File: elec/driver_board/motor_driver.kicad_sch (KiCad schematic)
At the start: 7 parts, among them IC25 MC74HC595ADR2G-Q, IC26 TPL7407LADR, IC27 TPL7407LADR, J15 MOTOR_1, J16 MOTOR_0

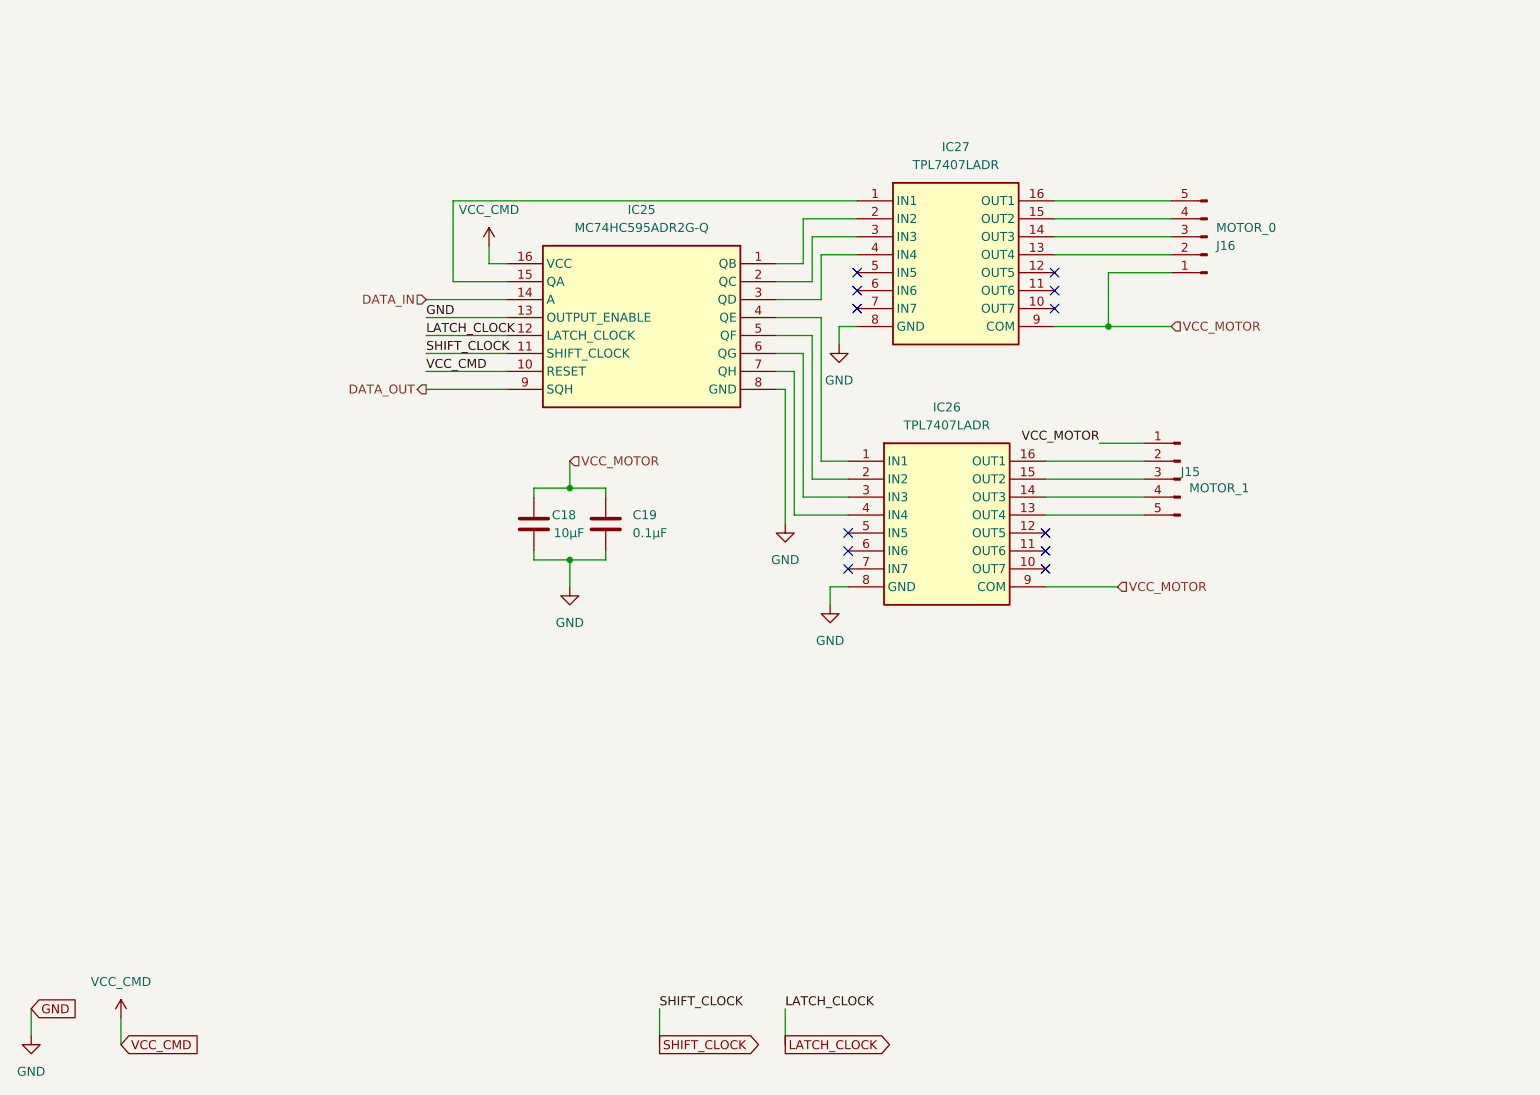
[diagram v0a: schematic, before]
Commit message: [elec] New design with BKA30D-R5
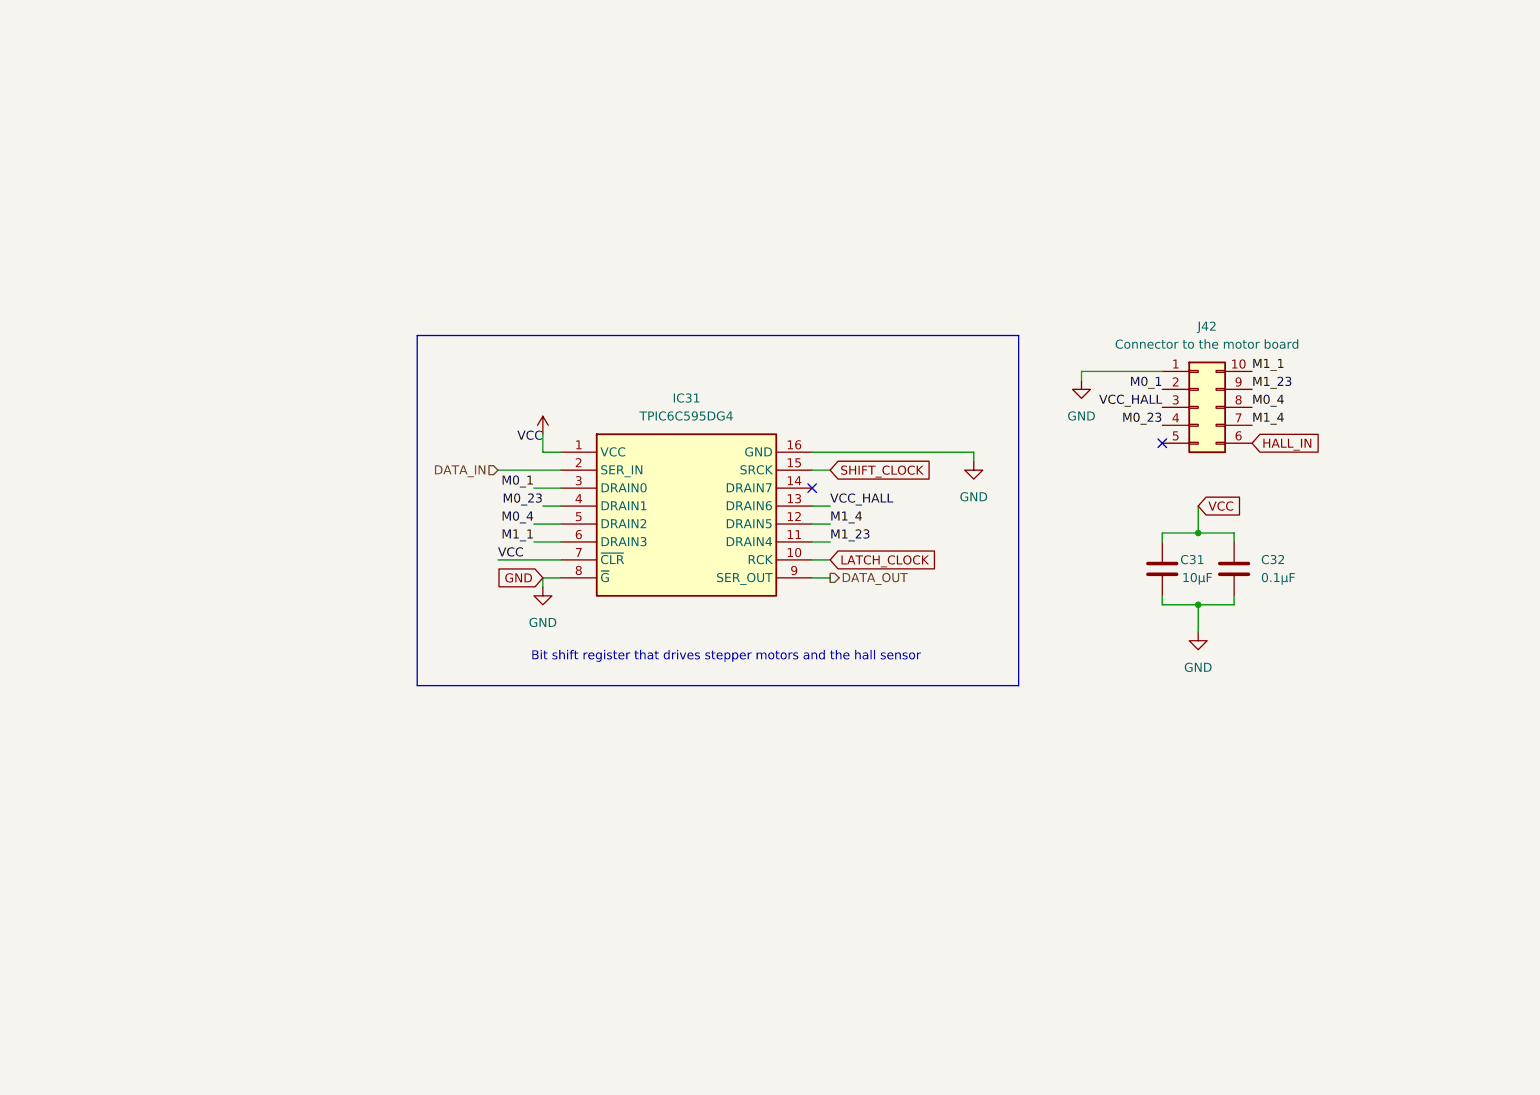
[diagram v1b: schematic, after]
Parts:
- removed IC25: MC74HC595ADR2G-Q, Samacsys:SOIC127P600X175-16N, symbol Samacsys:MC74HC595ADR2G-Q
- removed IC26, IC27: TPL7407LADR, Samacsys:SOIC127P600X175-16N, symbol Samacsys:TPL7407LADR
- removed J15: MOTOR_1, Connector_PinHeader_2.54mm:PinHeader_1x05_P2.54mm_Vertical, symbol Connector:Conn_01x05_Pin
- removed J16: MOTOR_0, Connector_PinHeader_2.54mm:PinHeader_1x05_P2.54mm_Vertical, symbol Connector:Conn_01x05_Pin
- added IC31: TPIC6C595DG4, Samacsys:SOIC127P600X175-16N, symbol Samacsys:TPIC6C595DG4
- added J42: Connector to the motor board, Connector_IDC:IDC-Header_2x05_P2.54mm_Vertical, symbol Connector_Generic:Conn_02x05_Counter_Clockwise
- renumbered C18 to C31, C19 to C32
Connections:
- net VCC_MOTOR is gone; now on net VCC_CMD: C31.1, C32.1
- net DATA_IN: now also IC31.2 (SER_IN)
- net DATA_OUT: now also IC31.9 (SER_OUT)
- net GND: now also IC31.16 (GND), IC31.8 (~{G}), J42.1 (Pin_1)
- net LATCH_CLOCK: now also IC31.10 (RCK)
- net SHIFT_CLOCK: now also IC31.15 (SRCK)
- net VCC_CMD: now also IC31.1 (VCC), IC31.7 (~{CLR})
- new net HALL_IN: J42.6 (Pin_6)
- new net M0_1: IC31.3 (DRAIN0), J42.2 (Pin_2)
- new net M0_23: IC31.4 (DRAIN1), J42.4 (Pin_4)
- new net M0_4: IC31.5 (DRAIN2), J42.8 (Pin_8)
- new net M1_1: IC31.6 (DRAIN3), J42.10 (Pin_10)
- new net M1_23: IC31.11 (DRAIN4), J42.9 (Pin_9)
- new net M1_4: IC31.12 (DRAIN5), J42.7 (Pin_7)
- new net VCC_HALL: IC31.13 (DRAIN6), J42.3 (Pin_3)
- no-connect marks 12 -> 2
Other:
- note added: "Bit shift register that drives stepper motors and the hall sensor"
- title: (none) -> Motor driver
- moved on the sheet: C31, C32

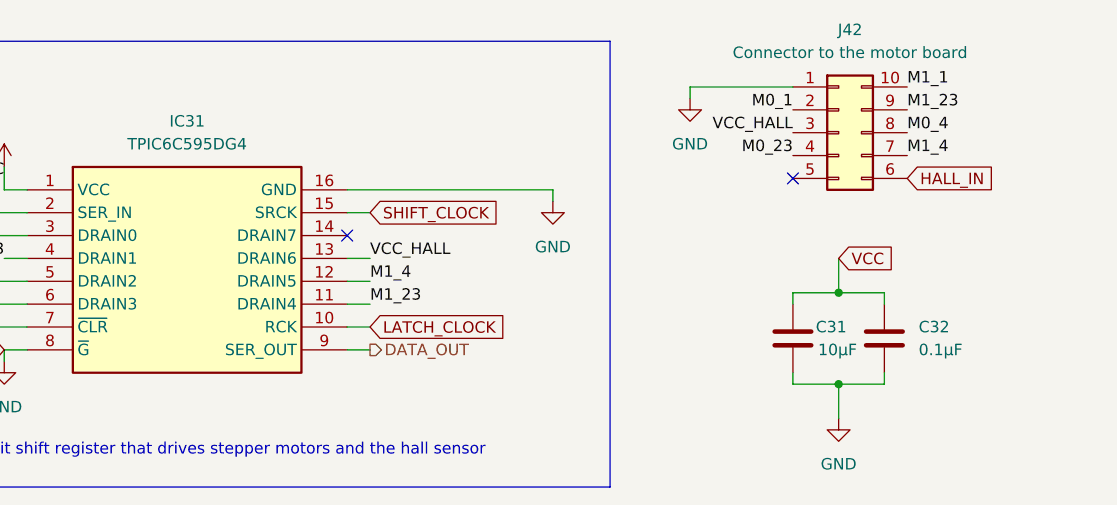
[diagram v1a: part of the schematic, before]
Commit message: [elec] continue routing
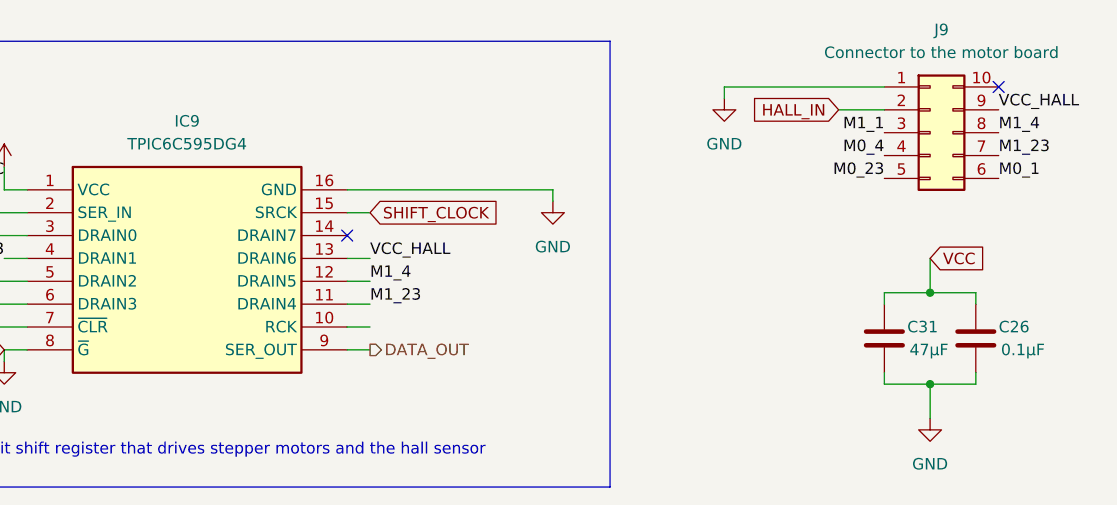
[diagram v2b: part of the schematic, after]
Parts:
- removed C32: 0.1µF, Snapeda:1808J1000392KCT_CAPC4520X200N, symbol Device:C
- added C26: 0.1µF, Capacitor_SMD:C_1210_3225Metric_Pad1.33x2.70mm_HandSolder, symbol Device:C
- C31: value 10µF -> 47µF; footprint Capacitor_SMD:C_1210_3225Metric -> Capacitor_SMD:C_1210_3225Metric_Pad1.33x2.70mm_HandSolder
- J9: renamed from J42; footprint Connector_IDC:IDC-Header_2x05_P2.54mm_Vertical -> Connector_JST:JST_PH_B10B-PH-K_1x10_P2.00mm_Vertical
- renumbered IC31 to IC9
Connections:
- net GND: now also C26.2
- net HALL_IN: now also J9.2 (Pin_2); no longer J9.6 (Pin_6)
- net M0_1: now also J9.6 (Pin_6); no longer J9.2 (Pin_2)
- net M0_23: now also J9.5 (Pin_5); no longer J9.4 (Pin_4)
- net M0_4: now also J9.4 (Pin_4); no longer J9.8 (Pin_8)
- net M1_1: now also J9.3 (Pin_3); no longer J9.10 (Pin_10)
- net M1_23: now also J9.7 (Pin_7); no longer J9.9 (Pin_9)
- net M1_4: now also J9.8 (Pin_8); no longer J9.7 (Pin_7)
- net VCC_CMD: now also C26.1
- net VCC_HALL: now also J9.9 (Pin_9); no longer J9.3 (Pin_3)
- net LATCH_CLOCK: no longer names the net of IC9.10 (RCK)
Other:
- moved on the sheet: C31, J9

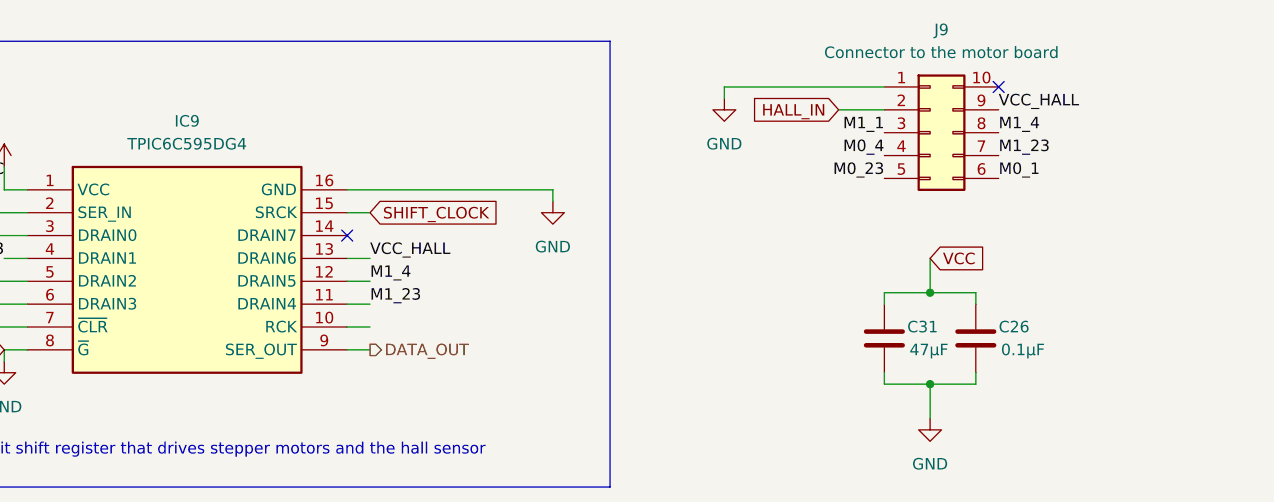
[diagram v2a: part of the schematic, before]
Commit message: [elec] First version of the routing of driver board
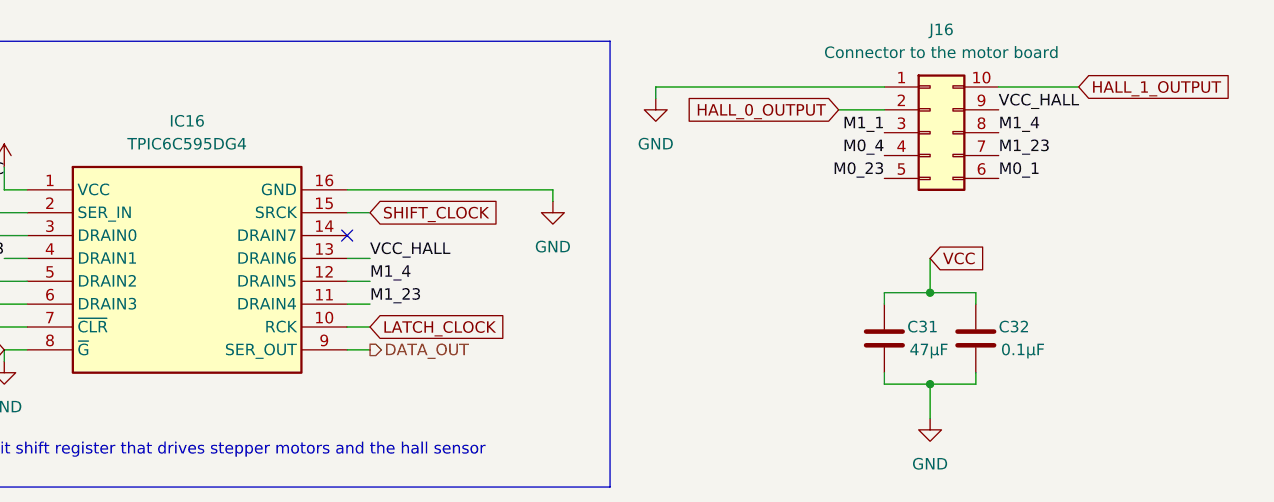
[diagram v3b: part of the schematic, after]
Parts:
- renumbered C26 to C32, IC9 to IC16, J9 to J16
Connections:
- net HALL_1_OUTPUT: now reaches J16.10 (Pin_10)
- net LATCH_CLOCK: now reaches IC16.10 (RCK)
- net HALL_IN renamed HALL_0_OUTPUT
- no-connect marks 2 -> 1
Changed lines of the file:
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@@
-	)
-	(no_connect
-		(at 219.71 83.82)
 	)
 	(no_connect
@@
 	(wire
 		(pts
+			(xy 228.6 83.82) (xy 219.71 83.82)
+		)
+		(stroke
+			(width 0)
+			(type default)
+		)
+	)
+	(wire
+		(pts
 			(xy 109.22 102.87) (xy 111.76 102.87)
 		)
@@
 	(wire
 		(pts
-			(xy 189.23 85.09) (xy 189.23 83.82)
-		)
-		(stroke
-			(width 0)
-			(type default)
-		)
-	)
-	(wire
-		(pts
-			(xy 189.23 83.82) (xy 207.01 83.82)
+			(xy 181.61 85.09) (xy 181.61 83.82)
+		)
+		(stroke
+			(width 0)
+			(type default)
+		)
+	)
+	(wire
+		(pts
+			(xy 181.61 83.82) (xy 207.01 83.82)
 		)
 		(stroke
@@
 		)
 	)
-	(global_label "HALL_IN"
+	(global_label "HALL_0_OUTPUT"
 		(shape input)
 		(at 201.93 86.36 180)
@@
 		(property "Intersheetrefs" "${INTERSHEET_REFS}"
 			(at 218.7038 102.87 0)
+			(effects
+				(font
+					(size 1.27 1.27)
+				)
+				(justify left)
+				(hide yes)
+			)
+		)
+	)
+	(global_label "HALL_1_OUTPUT"
+		(shape input)
+		(at 228.6 83.82 0)
+		(fields_autoplaced yes)
+		(effects
+			(font
+				(size 1.27 1.27)
+			)
+			(justify left)
+		)
+		(property "Intersheetrefs" "${INTERSHEET_REFS}"
+			(at 246.4019 83.82 0)
+			(effects
+				(font
+					(size 1.27 1.27)
+				)
+				(justify left)
+				(hide yes)
+			)
+		)
+	)
+	(global_label "LATCH_CLOCK"
+		(shape input)
+		(at 149.86 110.49 0)
+		(fields_autoplaced yes)
+		(effects
+			(font
+				(size 1.27 1.27)
+			)
+			(justify left)
+		)
+		(property "Intersheetrefs" "${INTERSHEET_REFS}"
+			(at 165.6662 110.49 0)
 			(effects
 				(font
@@
 		(dnp no)
 		(fields_autoplaced yes)
-		(property "Reference" "#PWR043"
+		(property "Reference" "#PWR078"
 			(at 170.18 102.87 0)
 			(effects
@@
 		(dnp no)
 		(fields_autoplaced yes)
-		(property "Reference" "#PWR041"
+		(property "Reference" "#PWR076"
 			(at 109.22 96.52 0)
 			(effects
@@
 		(dnp no)
 		(fields_autoplaced yes)
-		(property "Reference" "J9"
+		(property "Reference" "J16"
 			(at 213.36 77.47 0)
 			(effects
@@
 		(dnp no)
 		(fields_autoplaced yes)
-		(property "Reference" "IC9"
+		(property "Reference" "IC16"
 			(at 129.54 87.63 0)
 			(effects
@@
 		(dnp no)
 		(fields_autoplaced yes)
-		(property "Reference" "#PWR042"
+		(property "Reference" "#PWR077"
 			(at 109.22 120.65 0)
 			(effects
@@
 		(dnp no)
 		(fields_autoplaced yes)
-		(property "Reference" "#PWR045"
+		(property "Reference" "#PWR080"
 			(at 212.09 127 0)
 			(effects
@@
 	(symbol
 		(lib_id "power:GND")
-		(at 189.23 85.09 0)
+		(at 181.61 85.09 0)
 		(unit 1)
 		(exclude_from_sim no)
@@
 		(dnp no)
 		(fields_autoplaced yes)
-		(property "Reference" "#PWR044"
-			(at 189.23 91.44 0)
+		(property "Reference" "#PWR079"
+			(at 181.61 91.44 0)
 			(effects
 				(font
@@
 		)
 		(property "Value" "GND"
-			(at 189.23 90.17 0)
+			(at 181.61 90.17 0)
 			(effects
 				(font
@@
 		)
 		(property "Footprint" ""
-			(at 189.23 85.09 0)
+			(at 181.61 85.09 0)
 			(effects
 				(font
@@
 		)
 		(property "Datasheet" ""
-			(at 189.23 85.09 0)
+			(at 181.61 85.09 0)
 			(effects
 				(font
@@
 		)
 		(property "Description" "Power symbol creates a global label with name \"GND\" , ground"
-			(at 189.23 85.09 0)
+			(at 181.61 85.09 0)
 			(effects
 				(font
@@
 		(on_board yes)
 		(dnp no)
-		(property "Reference" "C26"
+		(property "Reference" "C32"
 			(at 219.71 110.49 0)
 			(effects

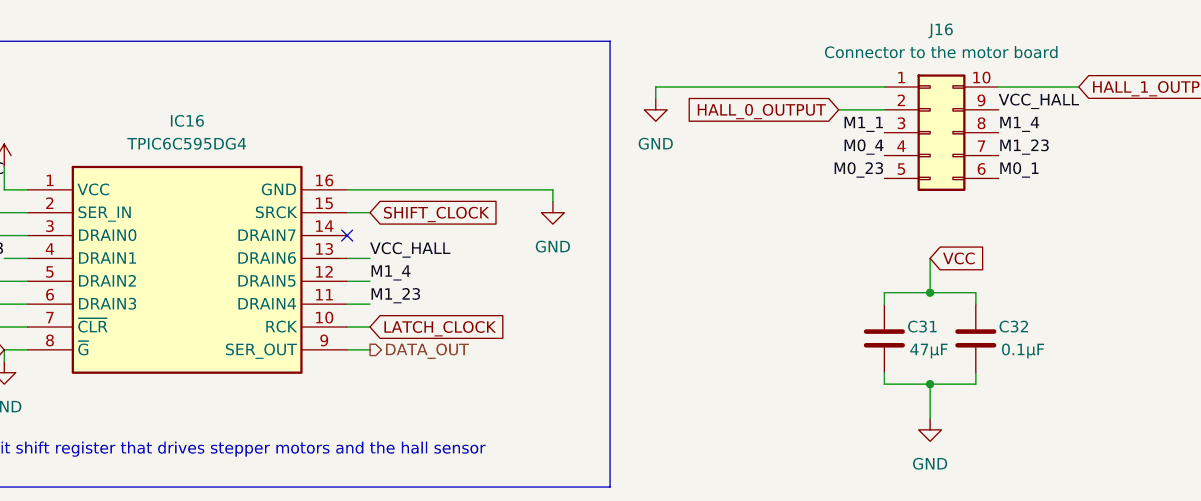
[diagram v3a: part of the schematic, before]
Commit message: [elec] Add space for physical button
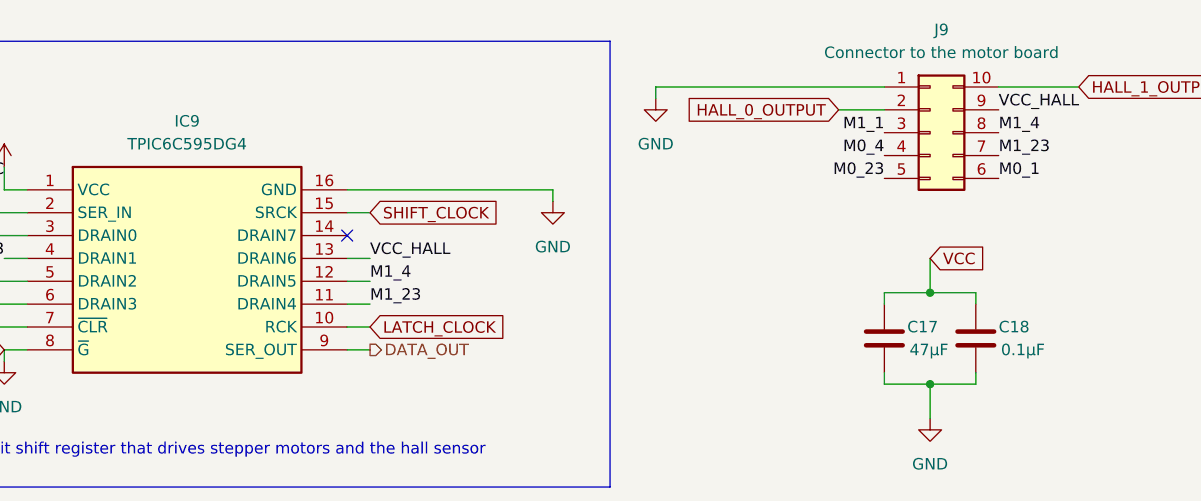
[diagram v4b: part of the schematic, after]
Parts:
- renumbered C31 to C17, C32 to C18, IC16 to IC9, J16 to J9
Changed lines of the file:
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@@
 		(dnp no)
 		(fields_autoplaced yes)
-		(property "Reference" "#PWR078"
+		(property "Reference" "#PWR043"
 			(at 170.18 102.87 0)
 			(effects
@@
 		(on_board yes)
 		(dnp no)
-		(property "Reference" "C31"
+		(property "Reference" "C17"
 			(at 209.55 110.49 0)
 			(effects
@@
 		(dnp no)
 		(fields_autoplaced yes)
-		(property "Reference" "#PWR076"
+		(property "Reference" "#PWR041"
 			(at 109.22 96.52 0)
 			(effects
@@
 		(dnp no)
 		(fields_autoplaced yes)
-		(property "Reference" "J16"
+		(property "Reference" "J9"
 			(at 213.36 77.47 0)
 			(effects
@@
 		(dnp no)
 		(fields_autoplaced yes)
-		(property "Reference" "IC16"
+		(property "Reference" "IC9"
 			(at 129.54 87.63 0)
 			(effects
@@
 		(dnp no)
 		(fields_autoplaced yes)
-		(property "Reference" "#PWR077"
+		(property "Reference" "#PWR042"
 			(at 109.22 120.65 0)
 			(effects
@@
 		(dnp no)
 		(fields_autoplaced yes)
-		(property "Reference" "#PWR080"
+		(property "Reference" "#PWR045"
 			(at 212.09 127 0)
 			(effects
@@
 		(dnp no)
 		(fields_autoplaced yes)
-		(property "Reference" "#PWR079"
+		(property "Reference" "#PWR044"
 			(at 181.61 91.44 0)
 			(effects
@@
 		(on_board yes)
 		(dnp no)
-		(property "Reference" "C32"
+		(property "Reference" "C18"
 			(at 219.71 110.49 0)
 			(effects
